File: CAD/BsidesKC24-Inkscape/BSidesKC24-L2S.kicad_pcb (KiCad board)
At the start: 2 copper layers, 63.5 x 99 mm, 15 parts, among them SW1 SW_SPST

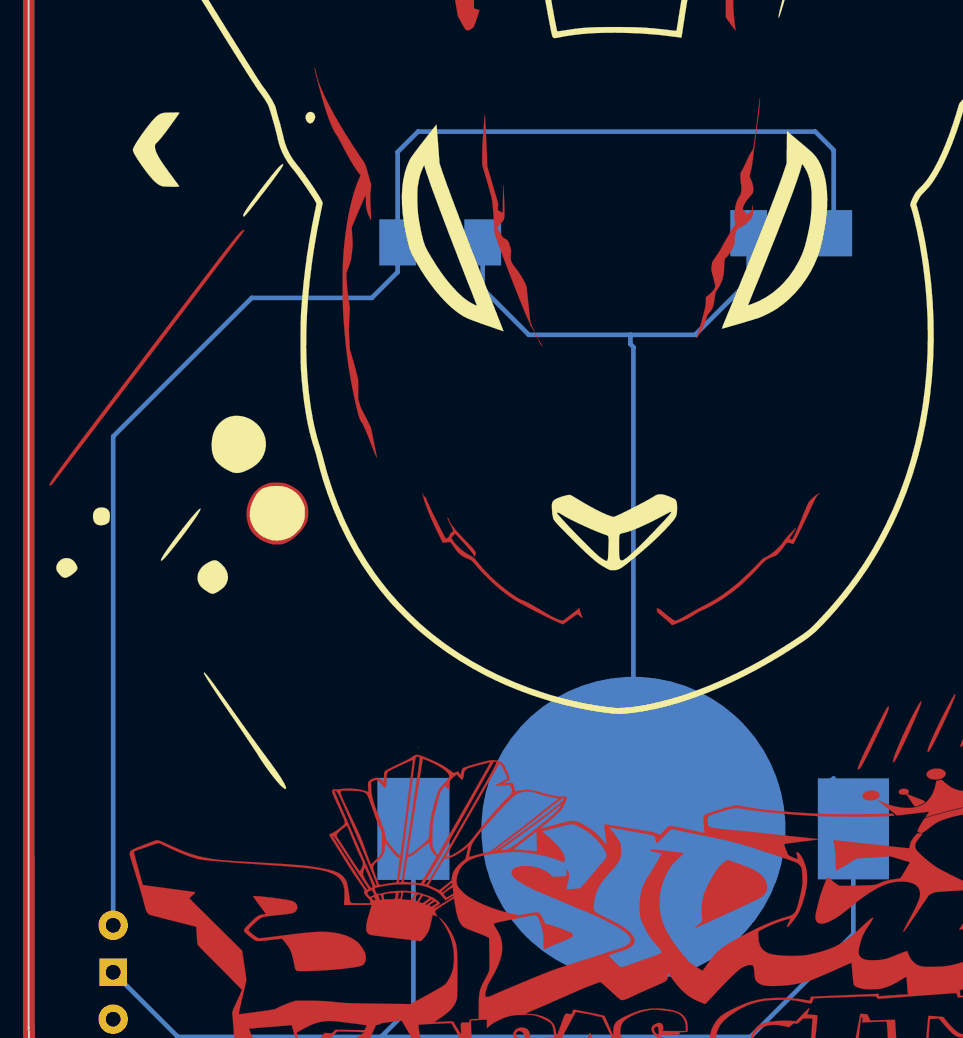
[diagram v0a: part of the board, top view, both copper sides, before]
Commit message: Parallel LEDs
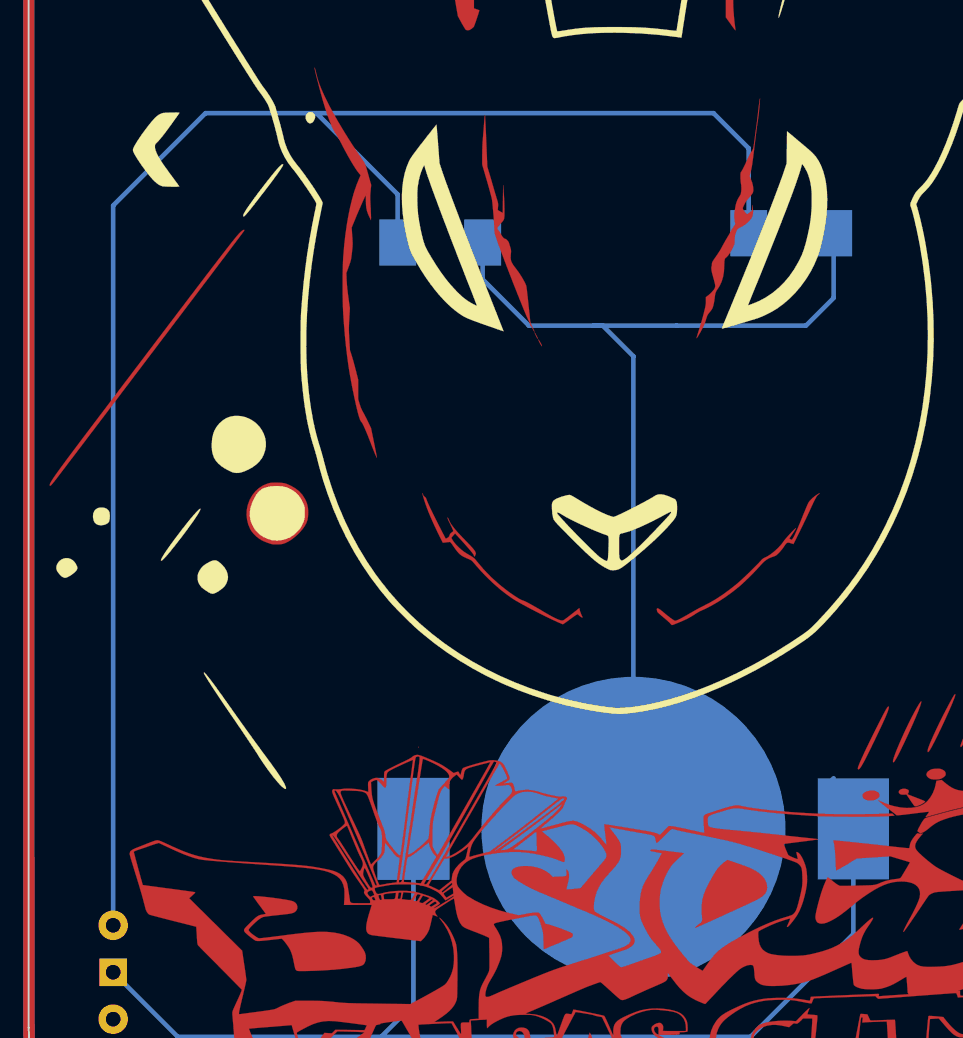
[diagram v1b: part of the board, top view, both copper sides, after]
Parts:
- turned D1 to 180 degrees
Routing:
- net Net-(D1-A): track 81.0 -> 89.6 mm
- net GND: track 48.5 -> 54.6 mm
